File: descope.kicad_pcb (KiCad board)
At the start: 2 copper layers, 26.9 x 31.8 mm, 19 parts, among them Q1 2N3906, Q2 2N3904, Q3 2N3906, Q4 2N3904, Q5 2N3906, Q6 2N3904

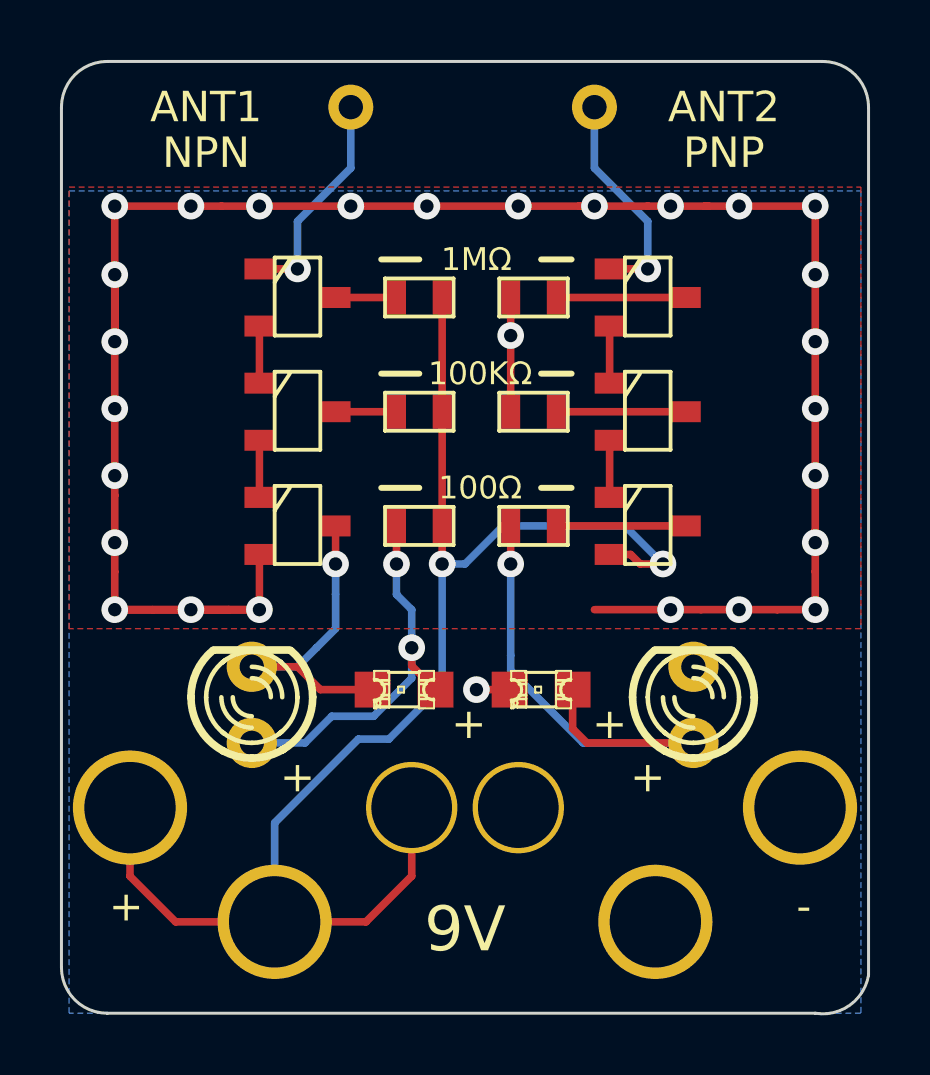
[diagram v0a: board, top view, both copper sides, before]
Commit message: Updated electroscope with pulled back copper pour
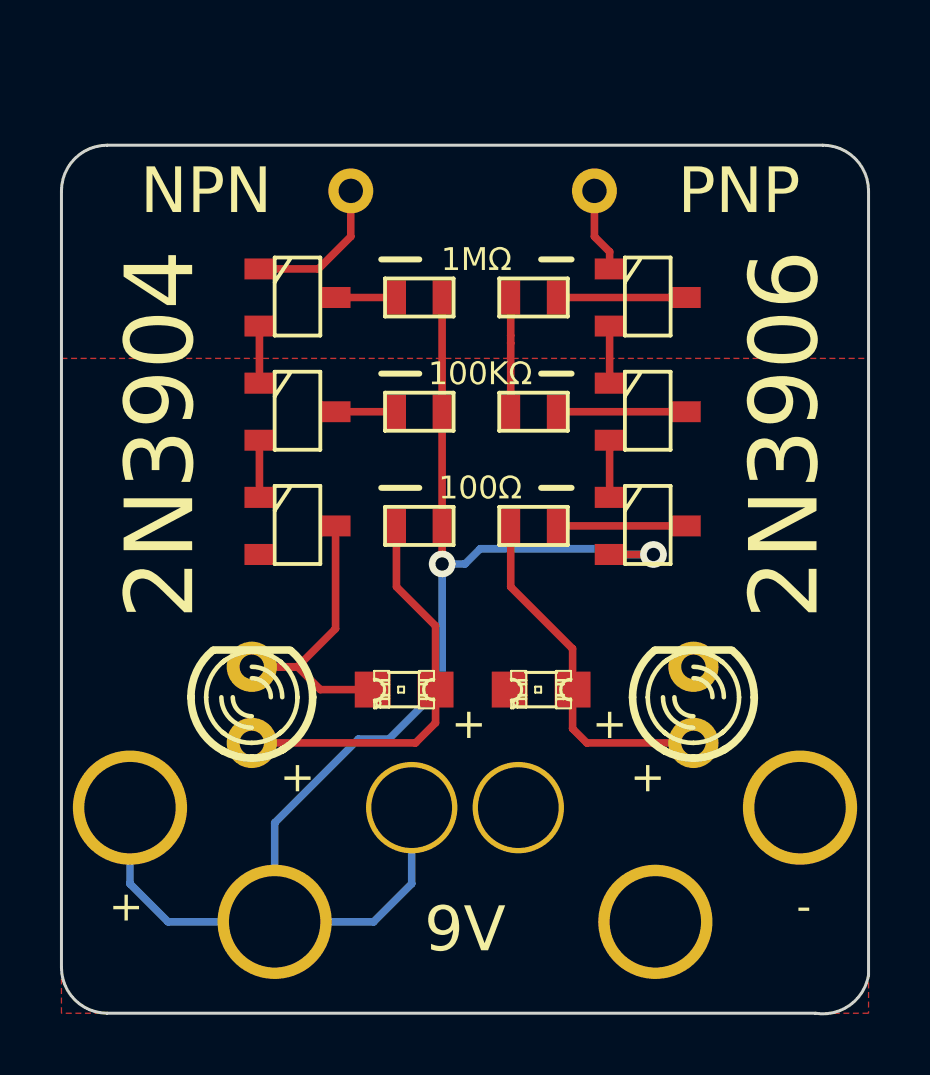
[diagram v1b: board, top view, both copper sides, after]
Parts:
- moved ANT1 2.79 mm to (152.7, 170.9)
- moved ANT2 2.79 mm to (160.8, 170.9)
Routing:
- net GND: track 80.8 -> 4.06 mm, vias 28 -> 0
- net N-000007: track 17.2 -> 11.8 mm, vias 1 -> 0
- net N-0000012: track 7.40 -> 2.81 mm, vias 1 -> 0
- net N-000001: track 7.40 -> 5.02 mm, vias 1 -> 0
- net VCC: track 49.0 -> 47.8 mm
- net N-0000011: track 13.0 -> 13.5 mm, vias 2 -> 0
- net N-000008: track 10.8 -> 11.1 mm, vias 1 -> 0
- removed copper zone on B.Cu, net GND
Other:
- board size 26.9 x 31.8 mm -> 26.9 x 29 mm
- board text added: "Differential Electroscope 2014-08-24"
- board text removed: "Toy Electroscope Git: 10acfe2 2014-05-14"
